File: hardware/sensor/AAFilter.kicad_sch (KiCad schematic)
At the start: 2 parts

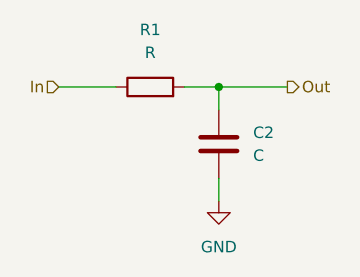
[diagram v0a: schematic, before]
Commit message: Implement filter in KiCad
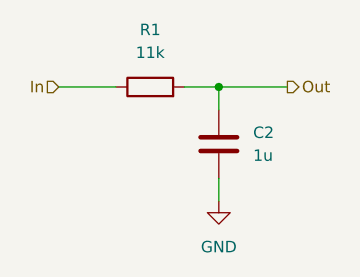
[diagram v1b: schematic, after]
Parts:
- C2: value C -> 1u
- R1: value R -> 11k
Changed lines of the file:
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@@
       (effects (font (size 1.27 1.27)) (justify left))
     )
-    (property "Value" "C" (at 110.49 71.12 0)
+    (property "Value" "1u" (at 110.49 71.12 0)
       (effects (font (size 1.27 1.27)) (justify left))
     )
@@
       (effects (font (size 1.27 1.27)))
     )
-    (property "Value" "R" (at 99.06 59.69 90)
+    (property "Value" "11k" (at 99.06 59.69 90)
       (effects (font (size 1.27 1.27)))
     )

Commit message: Fix incorrect upstream
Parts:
- added J501: ADC, testpoint_519x:Testpoint_519xTR, symbol Connector:Conn_01x01_Pin
- added J502: GND, testpoint_519x:Testpoint_519xTR, symbol Connector:Conn_01x01_Pin
- added J503: toDefboard, Connector_PinHeader_2.54mm:PinHeader_1x01_P2.54mm_Vertical, symbol Connector:Conn_01x01_Pin
- added JP501: SolderJumper_3_Open, Jumper:SolderJumper-3_P1.3mm_Open_RoundedPad1.0x1.5mm, symbol Jumper:SolderJumper_3_Open
- C501: renamed from C2; footprint (none) -> Capacitor_SMD:C_0805_2012Metric_Pad1.18x1.45mm_HandSolder
- R501: renamed from R1; footprint (none) -> Resistor_SMD:R_0805_2012Metric_Pad1.20x1.40mm_HandSolder
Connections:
- net GND: now also J502.1 (Pin_1)
- net Out: now also JP501.1 (A); no longer C501.1, R501.2
- new net: C501.1, J501.1 (Pin_1), JP501.2 (C), R501.2
- new net: J503.1 (Pin_1), JP501.3 (B)
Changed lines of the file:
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@@
   (junction (at 106.68 63.5) (diameter 0) (color 0 0 0 0)
   )
-  (wire (pts (xy 106.68 63.5) (xy 114.3 63.5))
+  (junction (at 111.76 57.15) (diameter 0) (color 0 0 0 0)
+  )
+  (junction (at 111.76 63.5) (diameter 0) (color 0 0 0 0)
+  )
+  (wire (pts (xy 134.62 54.61) (xy 138.43 54.61))
+    (stroke (width 0) (type default))
+  )
+  (wire (pts (xy 106.68 88.9) (xy 106.68 85.09))
+    (stroke (width 0) (type default))
+  )
+  (wire (pts (xy 134.62 68.58) (xy 134.62 74.93))
+    (stroke (width 0) (type default))
+  )
+  (wire (pts (xy 106.68 63.5) (xy 111.76 63.5))
+    (stroke (width 0) (type default))
+  )
+  (wire (pts (xy 134.62 74.93) (xy 140.97 74.93))
+    (stroke (width 0) (type default))
+  )
+  (wire (pts (xy 106.68 85.09) (xy 114.3 85.09))
+    (stroke (width 0) (type default))
+  )
+  (wire (pts (xy 111.76 57.15) (xy 114.3 57.15))
     (stroke (width 0) (type default))
   )
@@
     (stroke (width 0) (type default))
   )
+  (wire (pts (xy 134.62 58.42) (xy 134.62 54.61))
+    (stroke (width 0) (type default))
+  )
+  (wire (pts (xy 111.76 55.88) (xy 111.76 57.15))
+    (stroke (width 0) (type default))
+  )
   (wire (pts (xy 106.68 73.66) (xy 106.68 76.2))
+    (stroke (width 0) (type default))
+  )
+  (wire (pts (xy 111.76 57.15) (xy 111.76 63.5))
+    (stroke (width 0) (type default))
+  )
+  (wire (pts (xy 111.76 63.5) (xy 130.81 63.5))
     (stroke (width 0) (type default))
   )
@@
     (effects (font (size 1.27 1.27)) (justify right))
   )
-  (hierarchical_label "Out" (shape output) (at 114.3 63.5 0) (fields_autoplaced)
+  (hierarchical_label "Out" (shape output) (at 138.43 54.61 0) (fields_autoplaced)
     (effects (font (size 1.27 1.27)) (justify left))
   )
+  (netclass_flag "" (length 2.54) (shape round) (at 111.76 55.88 0) (fields_autoplaced)
+    (effects (font (size 1.27 1.27)) (justify left bottom))
+    (property "Netclass" "filter" (at 112.4585 53.34 0)
+      (effects (font (size 1.27 1.27) italic) (justify left))
+    )
+  )
   (symbol (lib_id "Device:C") (at 106.68 69.85 0) (unit 1)
     (in_bom yes) (on_board yes) (dnp no) (fields_autoplaced)
-    (property "Reference" "C2" (at 110.49 68.58 0)
+    (property "Reference" "C501" (at 110.49 68.58 0)
       (effects (font (size 1.27 1.27)) (justify left))
     )
@@
       (effects (font (size 1.27 1.27)) (justify left))
     )
-    (property "Footprint" "" (at 107.6452 73.66 0)
+    (property "Footprint" "Capacitor_SMD:C_0805_2012Metric_Pad1.18x1.45mm_HandSolder" (at 107.6452 73.66 0)
       (effects (font (size 1.27 1.27)) hide)
     )
@@
       (project "sensor"
         (path "/867f520a-eae4-4e8b-a296-c3a5e3f80a59/58c30a54-e504-4d13-8ccb-456e4733c866"
-          (reference "C2") (unit 1)
+          (reference "C501") (unit 1)
+        )
+      )
+    )
+  )
+  (symbol (lib_id "Connector:Conn_01x01_Pin") (at 119.38 85.09 180) (unit 1)
+    (in_bom yes) (on_board yes) (dnp no)
+    (property "Reference" "J502" (at 123.19 85.09 0)
+      (effects (font (size 1.27 1.27)))
+    )
+    (property "Value" "GND" (at 119.38 87.63 0)
+      (effects (font (size 1.27 1.27)))
+    )
+    (property "Footprint" "testpoint_519x:Testpoint_519xTR" (at 119.38 85.09 0)
+      (effects (font (size 1.27 1.27)) hide)
+    )
+    (property "Datasheet" "~" (at 119.38 85.09 0)
+      (effects (font (size 1.27 1.27)) hide)
+    )
+    (pin "1")
+    (instances
+      (project "sensor"
+        (path "/867f520a-eae4-4e8b-a296-c3a5e3f80a59/58c30a54-e504-4d13-8ccb-456e4733c866"
+          (reference "J502") (unit 1)
+        )
+      )
+    )
+  )
+  (symbol (lib_id "power:GND") (at 106.68 88.9 0) (unit 1)
+    (in_bom yes) (on_board yes) (dnp no) (fields_autoplaced)
+    (property "Reference" "#PWR0502" (at 106.68 95.25 0)
+      (effects (font (size 1.27 1.27)) hide)
+    )
+    (property "Value" "GND" (at 106.68 93.98 0)
+      (effects (font (size 1.27 1.27)))
+    )
+    (property "Footprint" "" (at 106.68 88.9 0)
+      (effects (font (size 1.27 1.27)) hide)
+    )
+    (property "Datasheet" "" (at 106.68 88.9 0)
+      (effects (font (size 1.27 1.27)) hide)
+    )
+    (pin "1")
+    (instances
+      (project "sensor"
+        (path "/867f520a-eae4-4e8b-a296-c3a5e3f80a59/58c30a54-e504-4d13-8ccb-456e4733c866"
+          (reference "#PWR0502") (unit 1)
         )
       )
@@
   (symbol (lib_id "power:GND") (at 106.68 76.2 0) (unit 1)
     (in_bom yes) (on_board yes) (dnp no) (fields_autoplaced)
-    (property "Reference" "#PWR06" (at 106.68 82.55 0)
+    (property "Reference" "#PWR0501" (at 106.68 82.55 0)
       (effects (font (size 1.27 1.27)) hide)
     )
@@
       (project "sensor"
         (path "/867f520a-eae4-4e8b-a296-c3a5e3f80a59/58c30a54-e504-4d13-8ccb-456e4733c866"
-          (reference "#PWR06") (unit 1)
+          (reference "#PWR0501") (unit 1)
         )
       )
@@
   )
   (symbol (lib_id "Device:R") (at 99.06 63.5 90) (unit 1)
-    (in_bom yes) (on_board yes) (dnp no) (fields_autoplaced)
-    (property "Reference" "R1" (at 99.06 57.15 90)
-      (effects (font (size 1.27 1.27)))
-    )
-    (property "Value" "11k" (at 99.06 59.69 90)
-      (effects (font (size 1.27 1.27)))
-    )
-    (property "Footprint" "" (at 99.06 65.278 90)
+    (in_bom yes) (on_board yes) (dnp no)
+    (property "Reference" "R501" (at 96.52 60.96 90)
+      (effects (font (size 1.27 1.27)))
+    )
+    (property "Value" "11k" (at 101.6 60.96 90)
+      (effects (font (size 1.27 1.27)))
+    )
+    (property "Footprint" "Resistor_SMD:R_0805_2012Metric_Pad1.20x1.40mm_HandSolder" (at 99.06 65.278 90)
       (effects (font (size 1.27 1.27)) hide)
     )
@@
       (project "sensor"
         (path "/867f520a-eae4-4e8b-a296-c3a5e3f80a59/58c30a54-e504-4d13-8ccb-456e4733c866"
-          (reference "R1") (unit 1)
-        )
-      )
+          (reference "R501") (unit 1)
+        )
+      )
+    )
+  )
+  (symbol (lib_id "Connector:Conn_01x01_Pin") (at 119.38 57.15 180) (unit 1)
+    (in_bom yes) (on_board yes) (dnp no)
+    (property "Reference" "J501" (at 123.19 57.15 0)
+      (effects (font (size 1.27 1.27)))
+    )
+    (property "Value" "ADC" (at 120.65 59.69 0)
+      (effects (font (size 1.27 1.27)))
+    )
+    (property "Footprint" "testpoint_519x:Testpoint_519xTR" (at 119.38 57.15 0)
+      (effects (font (size 1.27 1.27)) hide)
+    )
+    (property "Datasheet" "~" (at 119.38 57.15 0)
+      (effects (font (size 1.27 1.27)) hide)
+    )
+    (pin "1")
+    (instances
+      (project "sensor"
+        (path "/867f520a-eae4-4e8b-a296-c3a5e3f80a59/58c30a54-e504-4d13-8ccb-456e4733c866"
+          (reference "J501") (unit 1)
+        )
+      )
+    )
+  )
+  (symbol (lib_id "Jumper:SolderJumper_3_Open") (at 134.62 63.5 270) (unit 1)
+    (in_bom yes) (on_board yes) (dnp no) (fields_autoplaced)
+    (property "Reference" "JP501" (at 137.16 62.23 90)
+      (effects (font (size 1.27 1.27)) (justify left))
+    )
+    (property "Value" "SolderJumper_3_Open" (at 137.16 64.77 90)
+      (effects (font (size 1.27 1.27)) (justify left))
+    )
+    (property "Footprint" "Jumper:SolderJumper-3_P1.3mm_Open_RoundedPad1.0x1.5mm" (at 134.62 63.5 0)
+      (effects (font (size 1.27 1.27)) hide)
+    )
+    (property "Datasheet" "~" (at 134.62 63.5 0)
+      (effects (font (size 1.27 1.27)) hide)
+    )
+    (pin "3")
+    (pin "2")
+    (pin "1")
+    (instances
+      (project "sensor"
+        (path "/867f520a-eae4-4e8b-a296-c3a5e3f80a59/58c30a54-e504-4d13-8ccb-456e4733c866"
+          (reference "JP501") (unit 1)
+        )
+      )
+    )
+  )
+  (symbol (lib_id "Connector:Conn_01x01_Pin") (at 146.05 74.93 180) (unit 1)
+    (in_bom yes) (on_board yes) (dnp no)
+    (property "Reference" "J503" (at 149.86 74.93 0)
+      (effects (font (size 1.27 1.27)))
+    )
+    (property "Value" "toDefboard" (at 147.32 77.47 0)
+      (effects (font (size 1.27 1.27)))
+    )
+    (property "Footprint" "Connector_PinHeader_2.54mm:PinHeader_1x01_P2.54mm_Vertical" (at 146.05 74.93 0)
+      (effects (font (size 1.27 1.27)) hide)
+    )
+    (property "Datasheet" "~" (at 146.05 74.93 0)
+      (effects (font (size 1.27 1.27)) hide)
+    )
+    (pin "1")
+    (instances
+      (project "sensor"
+        (path "/867f520a-eae4-4e8b-a296-c3a5e3f80a59/58c30a54-e504-4d13-8ccb-456e4733c866"
+          (reference "J503") (unit 1)
+        )
+      )

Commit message: Add bom and final version of rev 1.0
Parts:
- C501: Digikey (none) -> 1276-6471-1-ND
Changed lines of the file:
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@@
       (effects (font (size 1.27 1.27)) hide)
     )
-    (property "Datasheet" "~" (at 106.68 69.85 0)
+    (property "Datasheet" "http://www.samsungsem.com/kr/support/product-search/mlcc/CL21B105KOFNNNG.jsp" (at 106.68 69.85 0)
+      (effects (font (size 1.27 1.27)) hide)
+    )
+    (property "Digikey" "1276-6471-1-ND" (at 106.68 69.85 0)
+      (effects (font (size 1.27 1.27)) hide)
+    )
+    (property "Farnell" "~" (at 106.68 69.85 0)
       (effects (font (size 1.27 1.27)) hide)
     )
@@
     )
     (property "Datasheet" "~" (at 119.38 85.09 0)
+      (effects (font (size 1.27 1.27)) hide)
+    )
+    (property "Digikey" "" (at 119.38 85.09 0)
       (effects (font (size 1.27 1.27)) hide)
     )
@@
       (effects (font (size 1.27 1.27)) hide)
     )
+    (property "Digikey" "" (at 99.06 63.5 0)
+      (effects (font (size 1.27 1.27)) hide)
+    )
     (pin "1")
     (pin "2")
@@
       (effects (font (size 1.27 1.27)) hide)
     )
+    (property "Digikey" "" (at 119.38 57.15 0)
+      (effects (font (size 1.27 1.27)) hide)
+    )
     (pin "1")
     (instances
@@
     )
     (property "Datasheet" "~" (at 134.62 63.5 0)
+      (effects (font (size 1.27 1.27)) hide)
+    )
+    (property "Digikey" "~" (at 134.62 63.5 0)
+      (effects (font (size 1.27 1.27)) hide)
+    )
+    (property "Farnell" "~" (at 134.62 63.5 0)
       (effects (font (size 1.27 1.27)) hide)
     )
@@
       (effects (font (size 1.27 1.27)) hide)
     )
+    (property "Digikey" "~" (at 146.05 74.93 0)
+      (effects (font (size 1.27 1.27)) hide)
+    )
+    (property "Farnell" "~" (at 146.05 74.93 0)
+      (effects (font (size 1.27 1.27)) hide)
+    )
